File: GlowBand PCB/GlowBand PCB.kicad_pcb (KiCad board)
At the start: 2 copper layers, 44 x 34.5 mm, 74 parts, among them P1 Solder_Pad, P2 Solder_Pad, P3 Solder_Pad, P4 Solder_Pad, P5 Solder_Pad, P6 Solder_Pad, P7 Solder_Pad, P8 Solder_Pad, P9 Magnetic Pogopin 6pin female, SW1 TS24CA, SW2 TS24CA, SW3 TS-1185EC-C-D-B, SW4 TS-1185EC-C-D-B, U1 ESP32-WROOM-32E, U10 SN74LVC1G373DBVR, U13 AP40P05, U15 MSM261D4030H1CPM, U16 AP40P05, U17 AO3400A, U18 FS8205A, U19 TP4056, U2 FXL0530-6R8-M, U20 DW01A, U3 SN74LVC2T45DCUR, U4 TPS61032PWPR, U5 AP40P05, U6 SS54, U7 SPX3819M5-L-3-3_TR, U9 AP40P05

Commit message: updated pcbs
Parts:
- added G***: LOGO, LOGO, B.Cu at (93.6, 63.2)
- SW3, SW4: moved to B.Cu
- moved SW4 67.5 mm to (81.3, 83.4), turned to 180 degrees
- moved JP1 43.8 mm to (105.0, 67.8)
- moved R16 42.6 mm to (113.2, 57.0), turned to 90 degrees
- moved C12 42.3 mm to (109.8, 66.3)
- moved C5 42.3 mm to (77.3, 63.4), turned to -90 degrees
- moved U9 42.3 mm to (108.2, 83.2)
- moved C16 42.1 mm to (82.5, 60.7), turned to 180 degrees
- moved R21 41.9 mm to (99.6, 77.7)
- moved R19 41.5 mm to (102.0, 77.7)
- moved C17 41.5 mm to (103.9, 77.7)
- moved R18 41.4 mm to (79.9, 58.0)
- moved R20 41.4 mm to (79.9, 59.0)
- moved F1 41.3 mm to (103.6, 82.5)
- moved R13 41.2 mm to (111.6, 84.0), turned to -90 degrees
- moved R12 41.2 mm to (112.7, 84.0)
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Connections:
- SW1 pad 3: GND -> +3V3
- SW2 pad 3: GND -> +3V3
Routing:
- net GND: track 0.00 -> 287.0 mm, vias 0 -> 28
- net +3V3: track 0.00 -> 103.4 mm, vias 0 -> 9
- net +5V: track 0.00 -> 86.8 mm, vias 0 -> 4
- net 3.3V AFTER MOSFET: track 0.00 -> 69.7 mm, vias 0 -> 9
- net 5V AFTER MOSFET: track 0.00 -> 60.9 mm, vias 0 -> 3
- net VBUS: track 0.00 -> 57.6 mm, vias 0 -> 4
- net IO14/SCK/TMS: track 0.00 -> 55.4 mm, vias 0 -> 7
- net LED1 DATA OUT: track 0.00 -> 51.9 mm, vias 0 -> 4
- net +BATT: track 0.00 -> 51.2 mm, vias 0 -> 4
- net IO4/BUTTON2: track 0.00 -> 50.0 mm, vias 0 -> 4
- net IO15/WS/TDO: track 0.00 -> 49.8 mm, vias 0 -> 4
- net IO27/BATT CHARGING: track 0.00 -> 42.5 mm, vias 0 -> 4
- net IO26/BATT VOLT: track 0.00 -> 40.7 mm, vias 0 -> 2
- net IO33/MAINBUTTON: track 0.00 -> 40.5 mm, vias 0 -> 4
- net EN: track 0.00 -> 40.1 mm, vias 0 -> 1
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- added copper zone on B.Cu, net GND
- added copper zone on F.Cu, net GND
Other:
- board size 44 x 34.5 mm -> 44 x 34.4 mm
- board text added: "+ BATT"
- board text added: "- BATT"
- board text added: "3.3V OUT"
- board text added: "5V"
- board text added: "5V IN/OUT"
- board text added: "BOOT"
- board text added: "EN"
- board text added: "G"
- board text added: "GND"
- board text added: "GlowBand v1.0 beta 1"
- board text added: "IO0"
- board text added: "IO12/TDI"
- board text added: "IO13/TCK"
- board text added: "IO14/SCK/TMS"
- board text added: "IO15/WS/TDO"
- board text added: "IO16"
- board text added: "IO17"
- board text added: "IO33"
- board text added: "IO4"
- board text added: "JLCJLCJLCJLC"
- board text added: "Microphone on"
- board text added: "Place battery here. Make sure this PCB side is completely flat and cannot damage the battery."
- board text added: "RESET"
- board text added: "RX"
- board text added: "TX"
- board text added: "V"
- board text added: "https://bit.ly/ 3O7S2Tk"

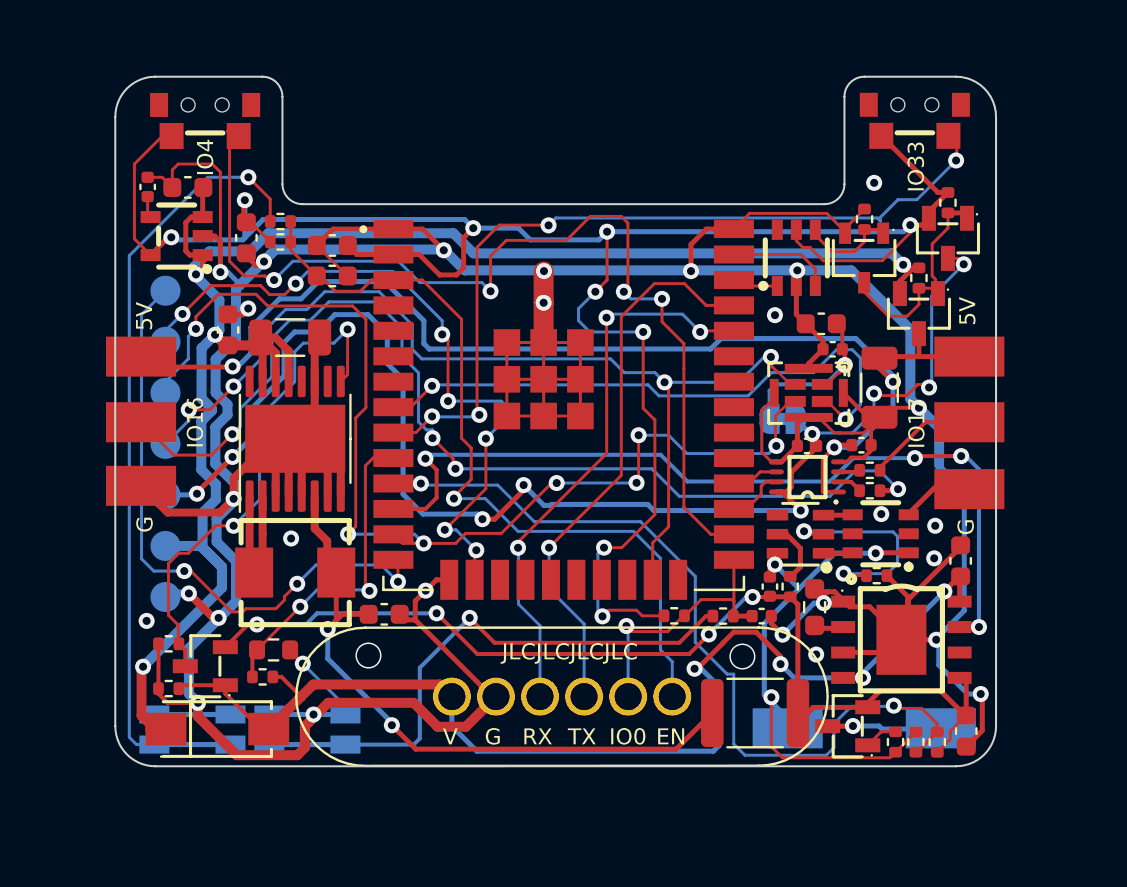
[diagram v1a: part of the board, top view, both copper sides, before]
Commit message: added gyroscope to GlowBand
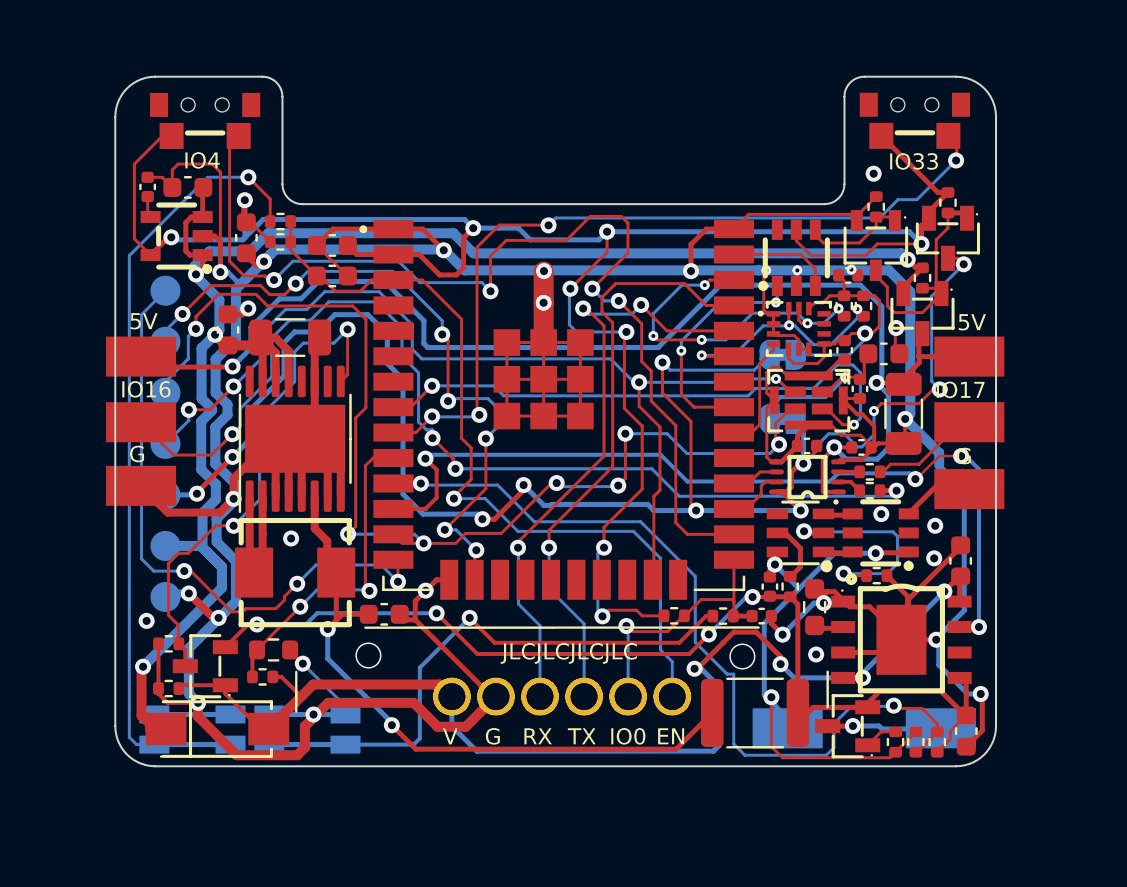
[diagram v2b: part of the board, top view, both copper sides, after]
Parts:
- added C10: 0.1uF, Capacitor_SMD:C_0402_1005Metric, F.Cu at (108.3, 60.7)
- added C11: 0.1uF, Capacitor_SMD:C_0402_1005Metric, F.Cu at (108.1, 64.4)
- added JP2: SolderJumper_2_Bridged, Jumper:SolderJumper-2_P1.3mm_Bridged_RoundedPad1.0x1.5mm, B.Cu at (105.0, 64.6)
- added R5: 10K, Resistor_SMD:R_0402_1005Metric, F.Cu at (109.0, 62.2)
- added R6: 10K, Resistor_SMD:R_0402_1005Metric, F.Cu at (108.1, 62.2)
- added U8: LSM6DS3TR-C, footprint:LGA-14_L3.0-W2.5-P0.50-TL, F.Cu at (105.8, 63.3)
- moved C15 3.47 mm to (110.0, 64.6), turned to 180 degrees
- moved C14 2.40 mm to (108.8, 66.3), turned to 90 degrees
- moved C12 1.78 mm to (111.0, 67.6)
- moved U17 0.85 mm to (109.6, 59.2)
- moved R15 0.85 mm to (109.7, 57.3)
- moved U15 0.38 mm to (106.3, 66.9)
- moved R14 0.18 mm to (112.0, 60.8)
- moved U13 0.18 mm to (112.0, 62.6)
- moved C2 0.11 mm to (108.9, 69.3)
- moved R2 0.08 mm to (109.3, 70.5)
- moved U20 0.07 mm to (105.9, 73.5)
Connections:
- U1 pad 30: unconnected-(U1-Pad30) -> IO18/I2C INT1
- U1 pad 31: unconnected-(U1-Pad31) -> IO19/LED LETCH EN
- U1 pad 33: unconnected-(U1-Pad33) -> IO21/I2C SDA
- U1 pad 36: IO22/LED LETCH EN -> IO22/I2C SCL
- U10 pad 1: IO22/LED LETCH EN -> IO19/LED LETCH EN
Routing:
- net IO22/I2C SCL: track 0.00 -> 17.8 mm, vias 0 -> 5
- net 3.3V AFTER MOSFET: track 69.7 -> 86.9 mm, vias 9 -> 11
- net GYRO VDD: track 0.00 -> 16.6 mm, vias 0 -> 1
- net IO21/I2C SDA: track 0.00 -> 12.8 mm, vias 0 -> 3
- net IO19/LED LETCH EN: track 0.00 -> 11.9 mm, vias 0 -> 2
- net GND: track 287.0 -> 295.9 mm, vias 28 -> 30
- net IO18/I2C INT1: track 0.00 -> 5.76 mm
- net 5V AFTER MOSFET: track 60.9 -> 64.7 mm
- net RXD0: track 28.0 -> 30.5 mm
- net IO22/LED LETCH EN: track 2.29 -> 0.00 mm
- net TXD0: track 27.9 -> 29.5 mm
- net IO4/BUTTON2: track 50.0 -> 51.4 mm
- net LED1 DATA OUT: track 51.9 -> 50.9 mm
- net IO15/WS/TDO: track 49.8 -> 49.0 mm
- net IO32/SD: track 30.1 -> 29.4 mm
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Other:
- board text added: "Gyroscope on"

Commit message: updated pinout
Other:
- board text added: "GlowBand v1.0 beta 2"
- board text removed: "GlowBand v1.0 beta 1"
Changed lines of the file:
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@@
     (effects (font (size 0.8 0.8) (thickness 0.15)) (justify right mirror))
   )
-  (gr_text "GlowBand\nv1.0 beta 1" (at 114.0968 60.2742) (layer "B.SilkS")
+  (gr_text "GlowBand\nv1.0 beta 2" (at 114.0968 60.2742) (layer "B.SilkS")
     (effects (font (size 1 1) (thickness 0.15)) (justify left mirror))
   )
@@
     (effects (font (size 0.8 0.8) (thickness 0.15)))
   )
-  (gr_text "G" (at 113.6142 69.723) (layer "F.SilkS")
+  (gr_text "GND" (at 112.649124 69.723) (layer "F.SilkS")
     (effects (font (size 0.8 0.8) (thickness 0.15)) (justify left))
   )
-  (gr_text "5V" (at 113.6904 63.0428) (layer "F.SilkS")
+  (gr_text "5V" (at 113.6396 63.0428) (layer "F.SilkS")
     (effects (font (size 0.8 0.8) (thickness 0.15)) (justify left))
   )
@@
     (effects (font (size 0.8 0.8) (thickness 0.15)))
   )
-  (gr_text "IO16" (at 71.9074 66.3956) (layer "F.SilkS")
+  (gr_text "IO16" (at 72.0344 66.3956) (layer "F.SilkS")
     (effects (font (size 0.8 0.8) (thickness 0.15)) (justify left))
   )
@@
     (effects (font (size 0.8 0.8) (thickness 0.15)))
   )
-  (gr_text "IO17" (at 112.5728 66.421) (layer "F.SilkS")
+  (gr_text "IO17" (at 112.344362 66.421) (layer "F.SilkS")
     (effects (font (size 0.8 0.8) (thickness 0.15)) (justify left))
   )
@@
     (effects (font (size 0.8 0.8) (thickness 0.15)))
   )
-  (gr_text "G" (at 72.3392 69.6214) (layer "F.SilkS")
+  (gr_text "GND" (at 72.0344 69.6214) (layer "F.SilkS")
     (effects (font (size 0.8 0.8) (thickness 0.15)) (justify left))
   )
-  (gr_text "5V" (at 72.3392 62.992) (layer "F.SilkS")
+  (gr_text "5V" (at 72.0344 62.992) (layer "F.SilkS")
     (effects (font (size 0.8 0.8) (thickness 0.15)) (justify left))
   )
